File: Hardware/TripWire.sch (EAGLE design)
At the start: 67 parts, among them P1 LSP11, P2 LSP11, P3 LSP11, P4 LSP11, P5 LSP11, P6 LSP11, P7 LSP11, X1 GADGETEER-SOCKET

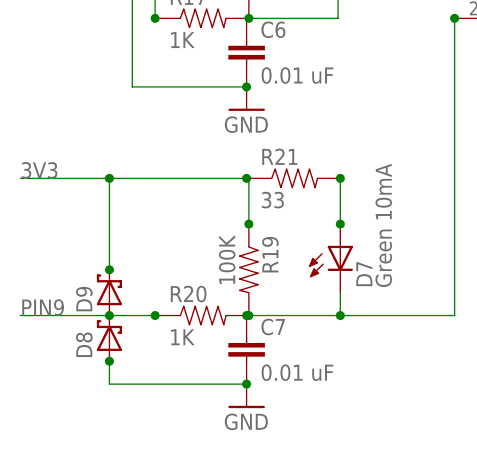
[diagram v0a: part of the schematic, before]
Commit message: Replaced single diodes with BAT42 custom part.
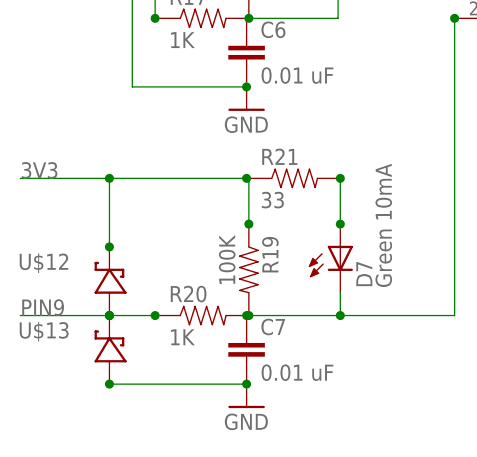
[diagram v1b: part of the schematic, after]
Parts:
- removed D8, D9: (no value), diode:SCHOTTKY-DIODESMD
- added U$12, U$13: BAT42-SCHOTTKY-DIODE, SoftDust:BAT42-SCHOTTKY-DIODE
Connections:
- net 3V3: now also U$12.P$1; no longer D9.C
- net GND: now also U$13.P$2; no longer D8.A
- net PIN9: now also U$12.P$2, U$13.P$1; no longer D8.C, D9.A
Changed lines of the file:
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@@
 <part name="U$10" library="SoftDust" deviceset="BAT54SDW" device=""/>
 <part name="U$11" library="SoftDust" deviceset="BAT54SDW" device=""/>
-<part name="D8" library="diode" deviceset="SCHOTTKY-DIODE" device="SMD"/>
-<part name="D9" library="diode" deviceset="SCHOTTKY-DIODE" device="SMD"/>
+<part name="U$12" library="SoftDust" deviceset="BAT42-SCHOTTKY-DIODE" device=""/>
+<part name="U$13" library="SoftDust" deviceset="BAT42-SCHOTTKY-DIODE" device=""/>
 </parts>
 <sheets>
@@
 <instance part="U$10" gate="G$1" x="147.32" y="63.5"/>
 <instance part="U$11" gate="G$1" x="22.86" y="71.12"/>
-<instance part="D8" gate="G$1" x="17.78" y="15.24" rot="R90"/>
-<instance part="D9" gate="G$1" x="17.78" y="20.32" rot="R90"/>
+<instance part="U$12" gate="G$1" x="17.78" y="20.32"/>
+<instance part="U$13" gate="G$1" x="17.78" y="12.7"/>
 </instances>
 <busses>
@@
 <wire x1="33.02" y1="33.02" x2="17.78" y2="33.02" width="0.1524" layer="91"/>
 <wire x1="17.78" y1="33.02" x2="7.874" y2="33.02" width="0.1524" layer="91"/>
-<wire x1="17.78" y1="22.86" x2="17.78" y2="33.02" width="0.1524" layer="91"/>
 <junction x="17.78" y="33.02"/>
-<pinref part="D9" gate="G$1" pin="C"/>
-<junction x="17.78" y="22.86"/>
+<pinref part="U$12" gate="G$1" pin="P$1"/>
+<wire x1="17.78" y1="25.4" x2="17.78" y2="33.02" width="0.1524" layer="91"/>
+<junction x="17.78" y="25.4"/>
 </segment>
 </net>
@@
 <pinref part="GND9" gate="1" pin="GND"/>
 <wire x1="33.02" y1="10.16" x2="17.78" y2="10.16" width="0.1524" layer="91"/>
-<wire x1="17.78" y1="10.16" x2="17.78" y2="12.7" width="0.1524" layer="91"/>
 <junction x="33.02" y="10.16"/>
-<pinref part="D8" gate="G$1" pin="A"/>
-<junction x="17.78" y="12.7"/>
+<pinref part="U$13" gate="G$1" pin="P$2"/>
+<junction x="17.78" y="10.16"/>
 </segment>
 </net>
@@
 <wire x1="22.86" y1="17.78" x2="17.78" y2="17.78" width="0.1524" layer="91"/>
 <junction x="22.86" y="17.78"/>
-<pinref part="D9" gate="G$1" pin="A"/>
+<junction x="17.78" y="17.78"/>
+<pinref part="U$12" gate="G$1" pin="P$2"/>
+<pinref part="U$13" gate="G$1" pin="P$1"/>
 <wire x1="17.78" y1="17.78" x2="7.874" y2="17.78" width="0.1524" layer="91"/>
 <junction x="17.78" y="17.78"/>
-<pinref part="D8" gate="G$1" pin="C"/>
-</segment>
-</net>
+</segment>
+</net>

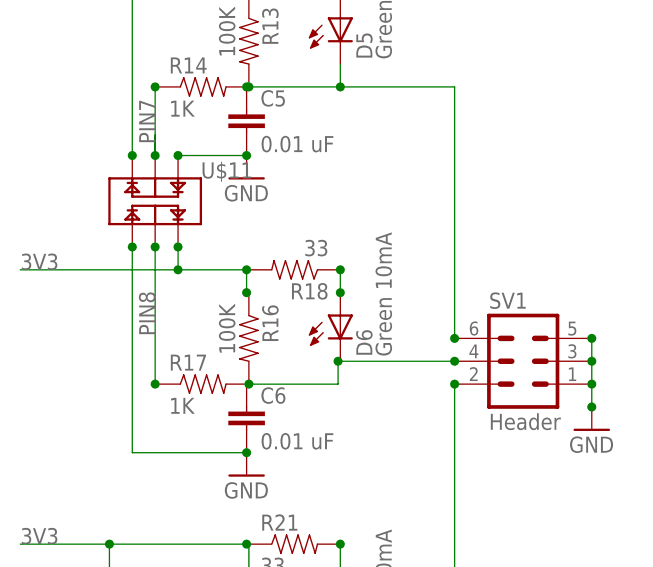
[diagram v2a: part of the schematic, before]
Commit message: Re-routed and all CRC checks resolved.
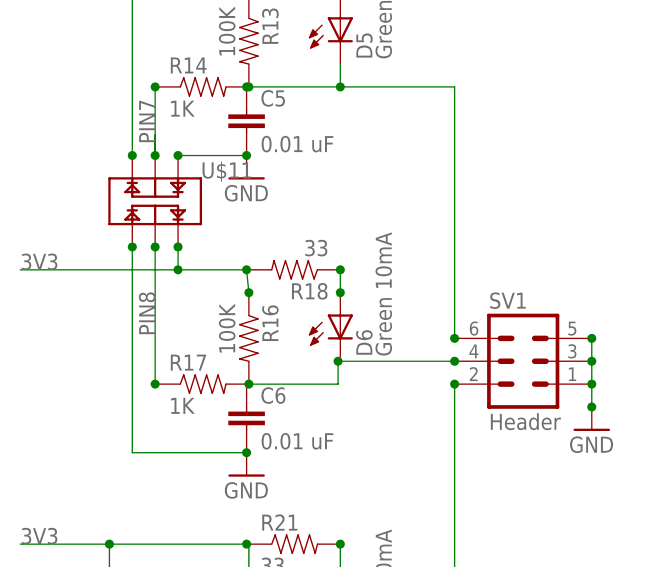
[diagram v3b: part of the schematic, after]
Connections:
- net 3V3: now also R16.1
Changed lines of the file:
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@@
 <?xml version="1.0" encoding="utf-8"?>
 <!DOCTYPE eagle SYSTEM "eagle.dtd">
-<eagle version="6.4">
+<eagle version="6.1">
 <drawing>
 <settings>
@@
 <wire x1="33.02" y1="63.5" x2="25.4" y2="63.5" width="0.1524" layer="91"/>
 <wire x1="25.4" y1="63.5" x2="7.874" y2="63.5" width="0.1524" layer="91"/>
-<wire x1="33.02" y1="60.96" x2="33.02" y2="63.5" width="0.1524" layer="91"/>
+<wire x1="33.274" y1="60.96" x2="33.02" y2="63.5" width="0.1524" layer="91"/>
 <junction x="33.02" y="63.5"/>
 <wire x1="25.4" y1="66.04" x2="25.4" y2="63.5" width="0.1524" layer="91"/>
 <junction x="25.4" y="63.5"/>
-<junction x="33.02" y="60.96"/>
 <pinref part="U$11" gate="G$1" pin="C1"/>
 <junction x="25.4" y="66.04"/>
+<pinref part="R16" gate="G$1" pin="1"/>
+<junction x="33.274" y="60.96"/>
 </segment>
 <segment>
@@
 </schematic>
 </drawing>
-<compatibility>
-<note version="6.3" minversion="6.2.2" severity="warning">
-Since Version 6.2.2 text objects can contain more than one line,
-which will not be processed correctly with this version.
-</note>
-</compatibility>
 </eagle>

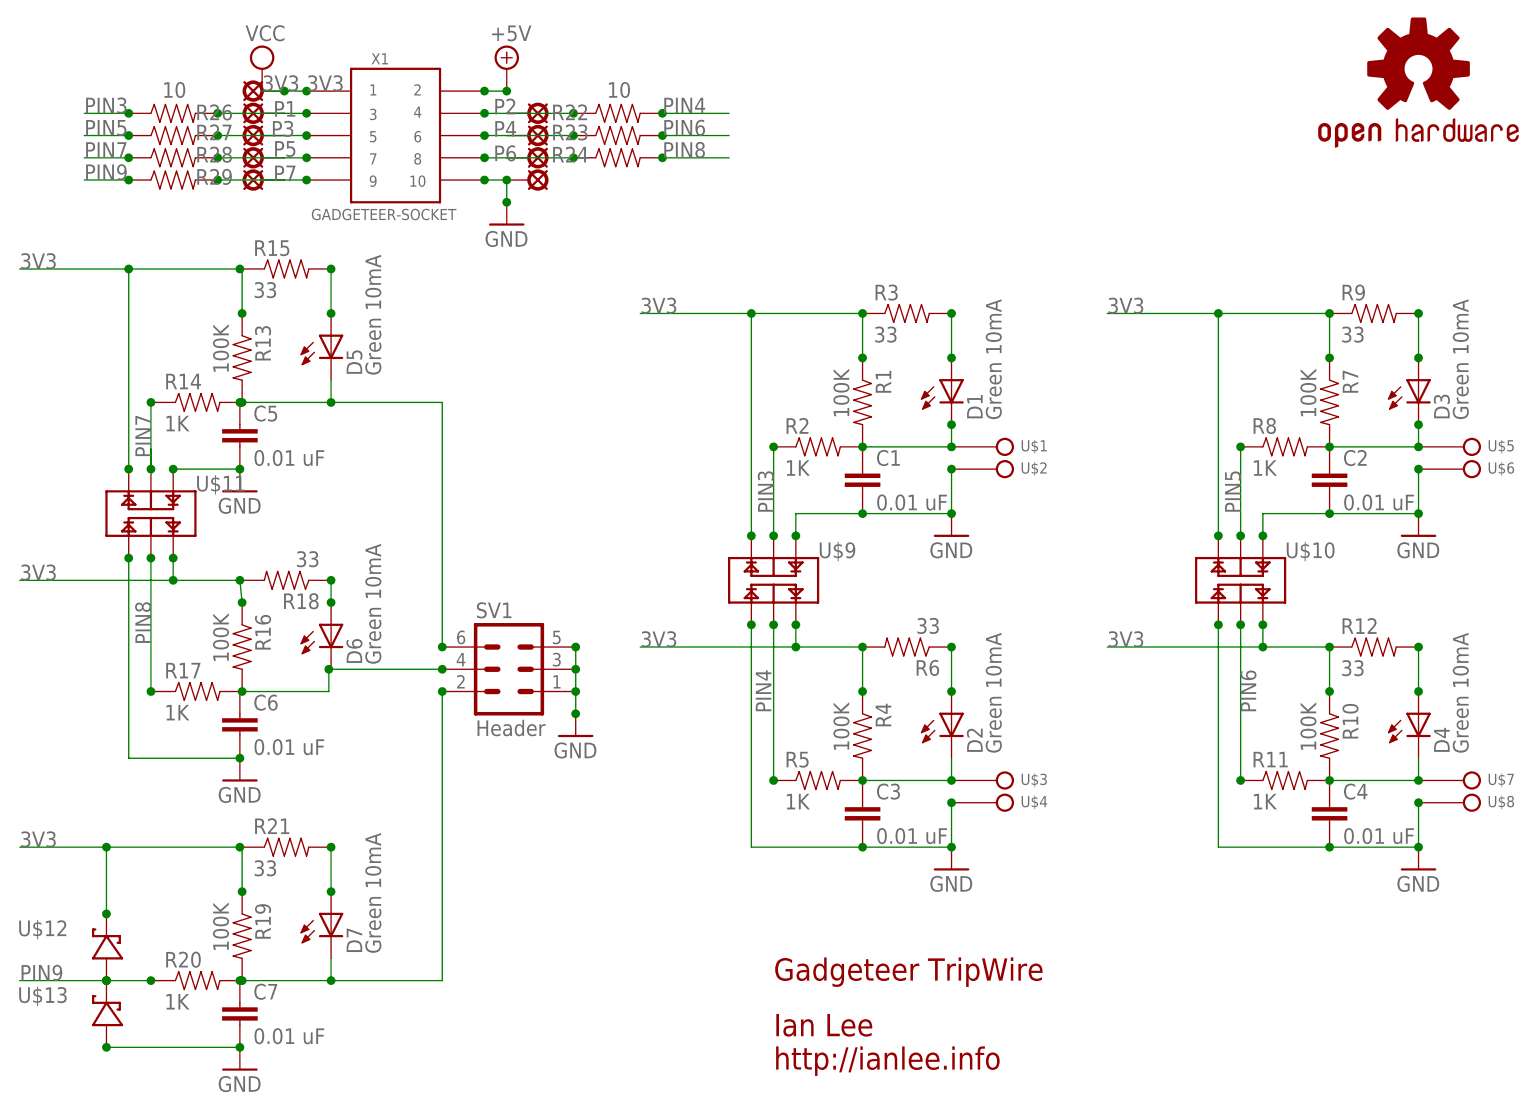
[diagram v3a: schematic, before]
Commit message: Moved C4.
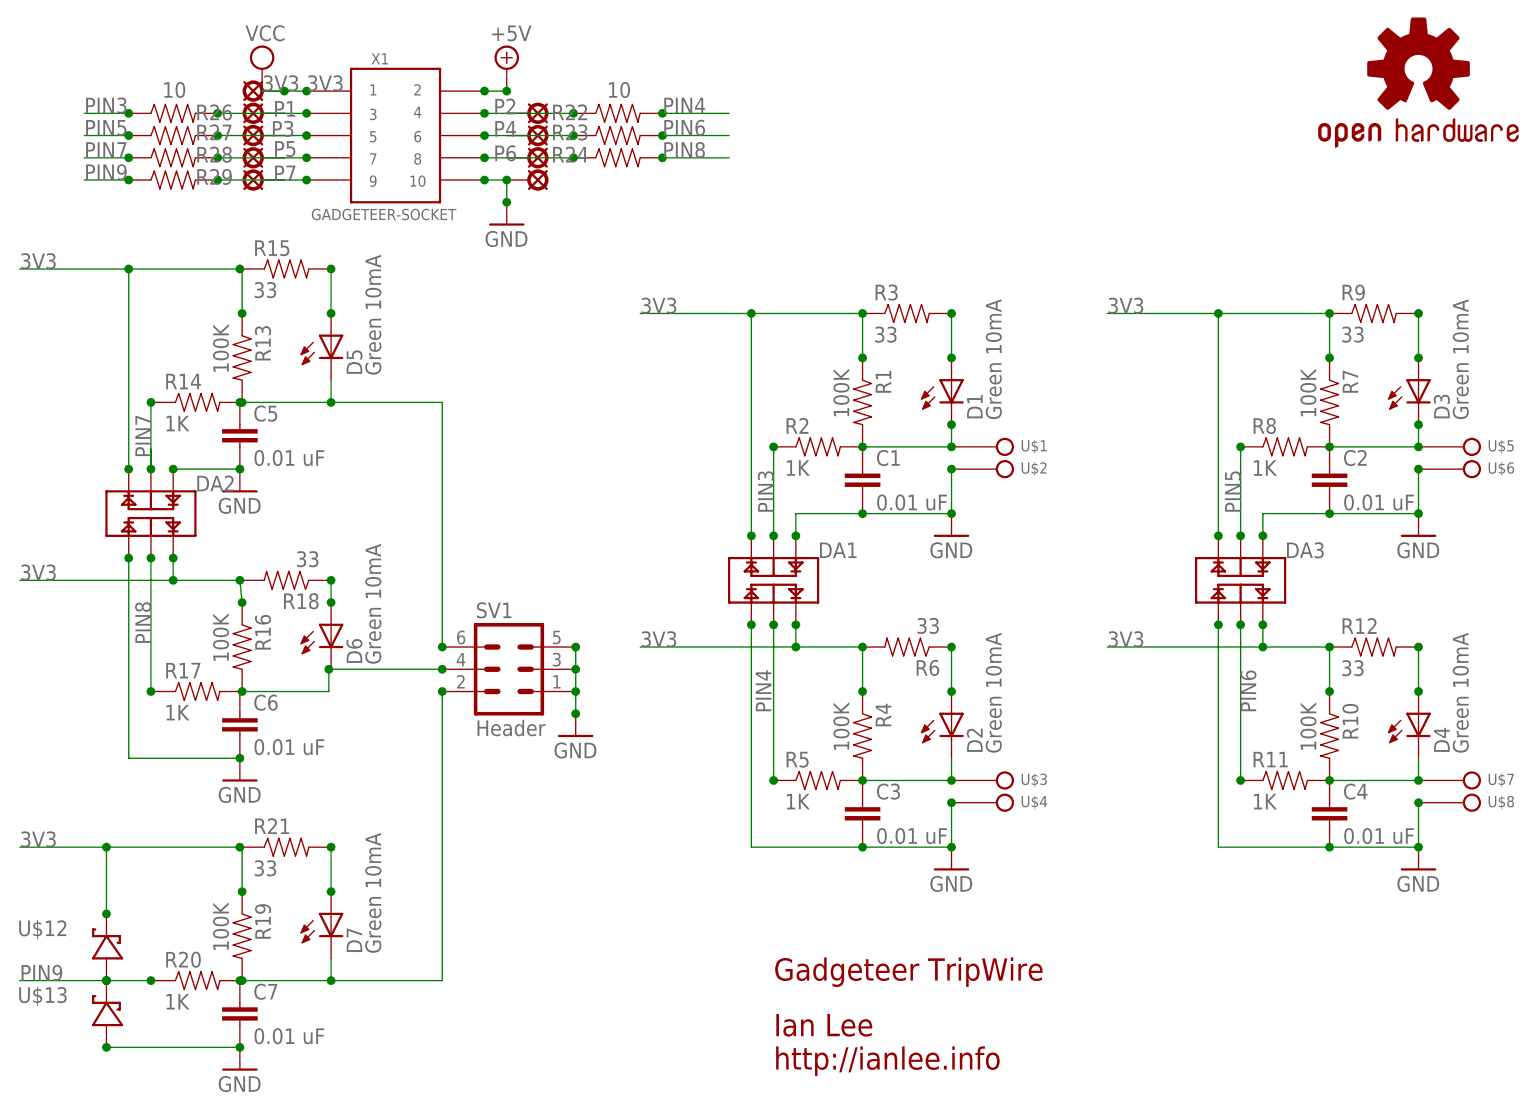
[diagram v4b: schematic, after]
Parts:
- renumbered U$10 to DA3, U$11 to DA2, U$9 to DA1
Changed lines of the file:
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@@
 <part name="C7" library="SparkFun-Capacitors" deviceset="CAP" device="0603-CAP" value="0.01 uF"/>
 <part name="GND9" library="supply1" deviceset="GND" device=""/>
-<part name="U$9" library="SoftDust" deviceset="BAT54SDW" device=""/>
-<part name="U$10" library="SoftDust" deviceset="BAT54SDW" device=""/>
-<part name="U$11" library="SoftDust" deviceset="BAT54SDW" device=""/>
+<part name="DA1" library="SoftDust" deviceset="BAT54SDW" device=""/>
+<part name="DA3" library="SoftDust" deviceset="BAT54SDW" device=""/>
+<part name="DA2" library="SoftDust" deviceset="BAT54SDW" device=""/>
 <part name="U$12" library="SoftDust" deviceset="BAT42-SCHOTTKY-DIODE" device=""/>
 <part name="U$13" library="SoftDust" deviceset="BAT42-SCHOTTKY-DIODE" device=""/>
@@
 <instance part="C7" gate="G$1" x="33.02" y="12.7"/>
 <instance part="GND9" gate="1" x="33.02" y="7.62"/>
-<instance part="U$9" gate="G$1" x="93.98" y="63.5"/>
-<instance part="U$10" gate="G$1" x="147.32" y="63.5"/>
-<instance part="U$11" gate="G$1" x="22.86" y="71.12"/>
+<instance part="DA1" gate="G$1" x="93.98" y="63.5"/>
+<instance part="DA3" gate="G$1" x="147.32" y="63.5"/>
+<instance part="DA2" gate="G$1" x="22.86" y="71.12"/>
 <instance part="U$12" gate="G$1" x="17.78" y="20.32"/>
 <instance part="U$13" gate="G$1" x="17.78" y="12.7"/>
@@
 <junction x="104.14" y="93.98"/>
 <junction x="104.14" y="88.9"/>
-<pinref part="U$9" gate="G$1" pin="C2"/>
+<pinref part="DA1" gate="G$1" pin="C2"/>
 <junction x="91.44" y="68.58"/>
 </segment>
@@
 <junction x="96.52" y="55.88"/>
 <junction x="104.14" y="50.8"/>
-<pinref part="U$9" gate="G$1" pin="C1"/>
+<pinref part="DA1" gate="G$1" pin="C1"/>
 <junction x="96.52" y="58.42"/>
 </segment>
@@
 <wire x1="144.78" y1="68.58" x2="144.78" y2="93.98" width="0.1524" layer="91"/>
 <junction x="144.78" y="93.98"/>
-<pinref part="U$10" gate="G$1" pin="C2"/>
+<pinref part="DA3" gate="G$1" pin="C2"/>
 <junction x="144.78" y="68.58"/>
 </segment>
@@
 <junction x="149.86" y="55.88"/>
 <junction x="157.48" y="50.8"/>
-<pinref part="U$10" gate="G$1" pin="C1"/>
+<pinref part="DA3" gate="G$1" pin="C1"/>
 <junction x="149.86" y="58.42"/>
 </segment>
@@
 <wire x1="20.32" y1="76.2" x2="20.32" y2="99.06" width="0.1524" layer="91"/>
 <junction x="20.32" y="99.06"/>
-<pinref part="U$11" gate="G$1" pin="C2"/>
+<pinref part="DA2" gate="G$1" pin="C2"/>
 <junction x="20.32" y="76.2"/>
 </segment>
@@
 <wire x1="25.4" y1="66.04" x2="25.4" y2="63.5" width="0.1524" layer="91"/>
 <junction x="25.4" y="63.5"/>
-<pinref part="U$11" gate="G$1" pin="C1"/>
+<pinref part="DA2" gate="G$1" pin="C1"/>
 <junction x="25.4" y="66.04"/>
 <pinref part="R16" gate="G$1" pin="1"/>
@@
 <junction x="114.3" y="71.12"/>
 <pinref part="C1" gate="G$1" pin="2"/>
-<pinref part="U$9" gate="G$1" pin="A2"/>
+<pinref part="DA1" gate="G$1" pin="A2"/>
 <wire x1="96.52" y1="68.58" x2="96.52" y2="71.12" width="0.1524" layer="91"/>
 <wire x1="96.52" y1="71.12" x2="104.14" y2="71.12" width="0.1524" layer="91"/>
@@
 <junction x="114.3" y="33.02"/>
 <junction x="114.3" y="38.1"/>
-<pinref part="U$9" gate="G$1" pin="A1"/>
+<pinref part="DA1" gate="G$1" pin="A1"/>
 <junction x="91.44" y="58.42"/>
 </segment>
@@
 <junction x="167.64" y="71.12"/>
 <junction x="167.64" y="76.2"/>
-<pinref part="U$10" gate="G$1" pin="A2"/>
+<pinref part="DA3" gate="G$1" pin="A2"/>
 <junction x="149.86" y="68.58"/>
 </segment>
@@
 <junction x="167.64" y="33.02"/>
 <junction x="167.64" y="38.1"/>
-<pinref part="U$10" gate="G$1" pin="A1"/>
+<pinref part="DA3" gate="G$1" pin="A1"/>
 <junction x="144.78" y="58.42"/>
 </segment>
@@
 <wire x1="25.4" y1="76.2" x2="33.02" y2="76.2" width="0.1524" layer="91"/>
 <junction x="33.02" y="76.2"/>
-<pinref part="U$11" gate="G$1" pin="A2"/>
+<pinref part="DA2" gate="G$1" pin="A2"/>
 <junction x="25.4" y="76.2"/>
 </segment>
@@
 <wire x1="20.32" y1="43.18" x2="20.32" y2="66.04" width="0.1524" layer="91"/>
 <junction x="33.02" y="43.18"/>
-<pinref part="U$11" gate="G$1" pin="A1"/>
+<pinref part="DA2" gate="G$1" pin="A1"/>
 <junction x="20.32" y="66.04"/>
 </segment>
@@
 <wire x1="93.98" y1="78.74" x2="93.98" y2="68.58" width="0.1524" layer="91"/>
 <junction x="93.98" y="78.74"/>
-<pinref part="U$9" gate="G$1" pin="AC2"/>
+<pinref part="DA1" gate="G$1" pin="AC2"/>
 <junction x="93.98" y="68.58"/>
 </segment>
@@
 <wire x1="93.98" y1="40.64" x2="93.98" y2="58.42" width="0.1524" layer="91"/>
 <junction x="93.98" y="40.64"/>
-<pinref part="U$9" gate="G$1" pin="AC1"/>
+<pinref part="DA1" gate="G$1" pin="AC1"/>
 <junction x="93.98" y="58.42"/>
 </segment>
@@
 <wire x1="147.32" y1="78.74" x2="147.32" y2="68.58" width="0.1524" layer="91"/>
 <junction x="147.32" y="78.74"/>
-<pinref part="U$10" gate="G$1" pin="AC2"/>
+<pinref part="DA3" gate="G$1" pin="AC2"/>
 <junction x="147.32" y="68.58"/>
 </segment>
@@
 <wire x1="22.86" y1="83.82" x2="22.86" y2="76.2" width="0.1524" layer="91"/>
 <junction x="22.86" y="83.82"/>
-<pinref part="U$11" gate="G$1" pin="AC2"/>
+<pinref part="DA2" gate="G$1" pin="AC2"/>
 <junction x="22.86" y="76.2"/>
 <wire x1="22.86" y1="76.2" x2="22.86" y2="78.486" width="0.1524" layer="91"/>
@@
 <wire x1="147.32" y1="40.64" x2="147.32" y2="58.42" width="0.1524" layer="91"/>
 <junction x="147.32" y="40.64"/>
-<pinref part="U$10" gate="G$1" pin="AC1"/>
+<pinref part="DA3" gate="G$1" pin="AC1"/>
 <junction x="147.32" y="58.42"/>
 </segment>
@@
 <wire x1="22.86" y1="50.8" x2="22.86" y2="66.04" width="0.1524" layer="91"/>
 <junction x="22.86" y="50.8"/>
-<pinref part="U$11" gate="G$1" pin="AC1"/>
+<pinref part="DA2" gate="G$1" pin="AC1"/>
 <junction x="22.86" y="66.04"/>
 </segment>

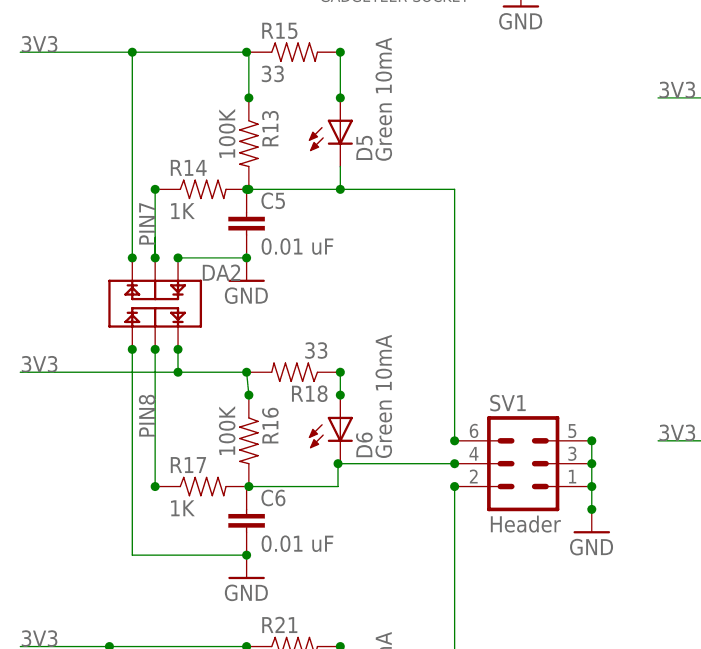
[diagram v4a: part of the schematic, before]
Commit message: Fixed bad connection on D6.
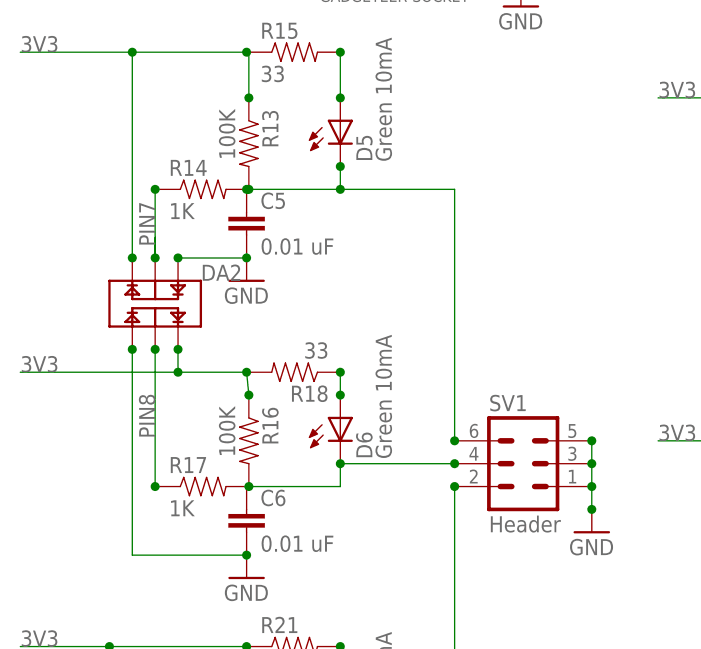
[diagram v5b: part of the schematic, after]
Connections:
- removed net N$23: C6.1, R16.2, R17.2
- net N$9: now also C6.1, R16.2, R17.2
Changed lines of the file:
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@@
 <wire x1="56.134" y1="53.34" x2="43.434" y2="53.34" width="0.1524" layer="91"/>
 <junction x="56.134" y="53.34"/>
+<pinref part="R16" gate="G$1" pin="2"/>
+<pinref part="R17" gate="G$1" pin="2"/>
+<junction x="33.274" y="50.8"/>
+<wire x1="33.274" y1="50.8" x2="33.02" y2="50.8" width="0.1524" layer="91"/>
+<pinref part="C6" gate="G$1" pin="1"/>
+<wire x1="33.02" y1="50.8" x2="43.434" y2="50.8" width="0.1524" layer="91"/>
+<wire x1="43.434" y1="50.8" x2="43.434" y2="53.34" width="0.1524" layer="91"/>
+<junction x="43.434" y="53.34"/>
 </segment>
 </net>
@@
 <pinref part="C5" gate="G$1" pin="1"/>
 <junction x="33.02" y="83.82"/>
+<junction x="43.434" y="86.36"/>
 </segment>
 </net>
@@
 </segment>
 </net>
-<net name="N$23" class="0">
-<segment>
-<pinref part="R16" gate="G$1" pin="2"/>
-<pinref part="R17" gate="G$1" pin="2"/>
-<junction x="33.274" y="50.8"/>
-<wire x1="33.274" y1="50.8" x2="33.02" y2="50.8" width="0.1524" layer="91"/>
-<pinref part="C6" gate="G$1" pin="1"/>
-<wire x1="33.02" y1="50.8" x2="43.18" y2="50.8" width="0.1524" layer="91"/>
-<wire x1="43.18" y1="50.8" x2="43.18" y2="53.34" width="0.1524" layer="91"/>
-<junction x="43.18" y="53.34"/>
-</segment>
-</net>
